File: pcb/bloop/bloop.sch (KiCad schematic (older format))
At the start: 10 parts

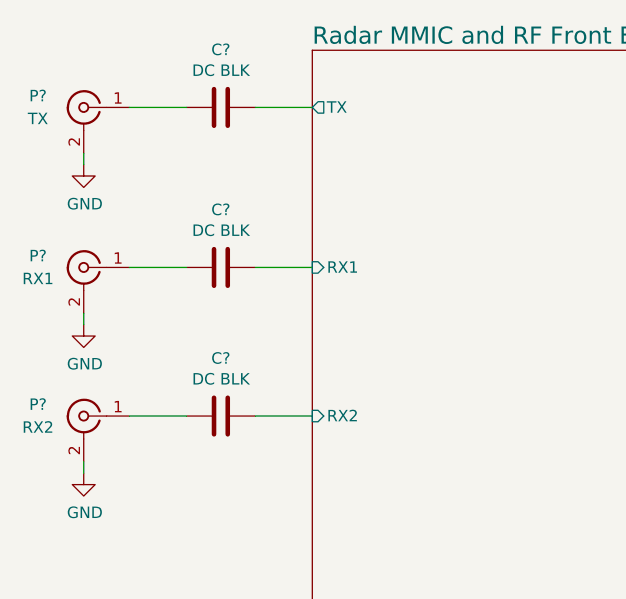
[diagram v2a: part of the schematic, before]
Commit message: Add stubs to RX portion; move blocking caps
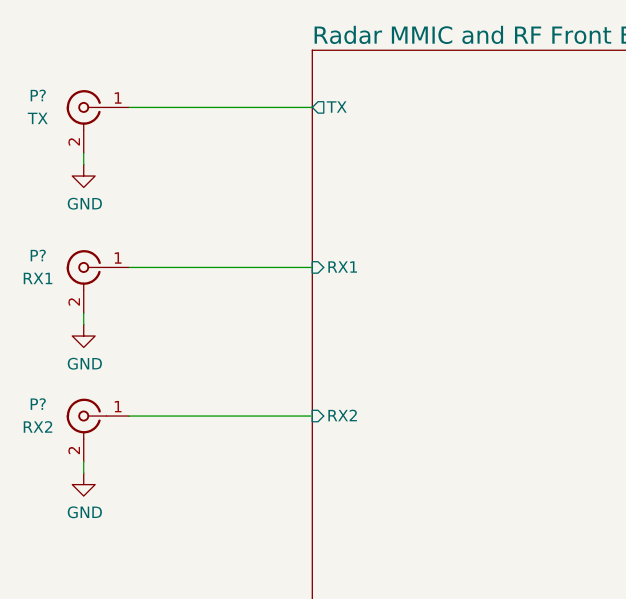
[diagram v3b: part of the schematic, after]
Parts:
- removed C? (x3): DC BLK, symbol Device:C
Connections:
- net Radar MMIC and RF Front End/RX1: now also P?.1 (In)
- net Radar MMIC and RF Front End/RX2: now also P?.1 (In)
- net Radar MMIC and RF Front End/TX: now also P?.1 (In)
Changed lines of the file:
@@
 EESchema Schematic File Version 4
 LIBS:bloop-cache
-EELAYER 29 0
+EELAYER 30 0
 EELAYER END
 $Descr B 17000 11000
@@
 	1    0    0    -1
 $EndComp
+$Comp
+L Mechanical:MountingHole_Pad H?
+U 1 1 5D89D33B
+P 11300 9750
+F 0 "H?" H 11400 9850 50  0000 L CNN
+F 1 "MNT_HOLE" H 11400 9750 50  0000 L CNN
+F 2 "" H 11300 9750 50  0001 C CNN
+F 3 "~" H 11300 9750 50  0001 C CNN
+	1    11300 9750
+	1    0    0    -1
+$EndComp
+$Comp
+L power:GND #PWR?
+U 1 1 5D89E2C2
+P 11300 9850
+F 0 "#PWR?" H 11300 9600 50  0001 C CNN
+F 1 "GND" H 11305 9677 50  0000 C CNN
+F 2 "" H 11300 9850 50  0001 C CNN
+F 3 "" H 11300 9850 50  0001 C CNN
+	1    11300 9850
+	1    0    0    -1
+$EndComp
+$Comp
+L Mechanical:MountingHole_Pad H?
+U 1 1 5D89F708
+P 10300 9750
+F 0 "H?" H 10400 9850 50  0000 L CNN
+F 1 "MNT_HOLE" H 10400 9750 50  0000 L CNN
+F 2 "" H 10300 9750 50  0001 C CNN
+F 3 "~" H 10300 9750 50  0001 C CNN
+	1    10300 9750
+	1    0    0    -1
+$EndComp
+$Comp
+L power:GND #PWR?
+U 1 1 5D89F70E
+P 10300 9850
+F 0 "#PWR?" H 10300 9600 50  0001 C CNN
+F 1 "GND" H 10305 9677 50  0000 C CNN
+F 2 "" H 10300 9850 50  0001 C CNN
+F 3 "" H 10300 9850 50  0001 C CNN
+	1    10300 9850
+	1    0    0    -1
+$EndComp
+$Comp
+L Mechanical:MountingHole_Pad H?
+U 1 1 5D8A33A6
+P 11300 8750
+F 0 "H?" H 11400 8850 50  0000 L CNN
+F 1 "MNT_HOLE" H 11400 8750 50  0000 L CNN
+F 2 "" H 11300 8750 50  0001 C CNN
+F 3 "~" H 11300 8750 50  0001 C CNN
+	1    11300 8750
+	1    0    0    -1
+$EndComp
+$Comp
+L power:GND #PWR?
+U 1 1 5D8A33AC
+P 11300 8850
+F 0 "#PWR?" H 11300 8600 50  0001 C CNN
+F 1 "GND" H 11305 8677 50  0000 C CNN
+F 2 "" H 11300 8850 50  0001 C CNN
+F 3 "" H 11300 8850 50  0001 C CNN
+	1    11300 8850
+	1    0    0    -1
+$EndComp
+$Comp
+L Mechanical:MountingHole_Pad H?
+U 1 1 5D8A33B2
+P 10300 8750
+F 0 "H?" H 10400 8850 50  0000 L CNN
+F 1 "MNT_HOLE" H 10400 8750 50  0000 L CNN
+F 2 "" H 10300 8750 50  0001 C CNN
+F 3 "~" H 10300 8750 50  0001 C CNN
+	1    10300 8750
+	1    0    0    -1
+$EndComp
+$Comp
+L power:GND #PWR?
+U 1 1 5D8A33B8
+P 10300 8850
+F 0 "#PWR?" H 10300 8600 50  0001 C CNN
+F 1 "GND" H 10305 8677 50  0000 C CNN
+F 2 "" H 10300 8850 50  0001 C CNN
+F 3 "" H 10300 8850 50  0001 C CNN
+	1    10300 8850
+	1    0    0    -1
+$EndComp
+Wire Notes Line
+	9600 8400 9600 10300
+Wire Notes Line
+	9600 10300 12000 10300
+Wire Notes Line
+	12000 10300 12000 8400
+Wire Notes Line
+	12000 8400 9600 8400
+Text Notes 10300 8300 0    100  ~ 20
+Mounting Holes
 $Sheet
 S 3900 3400 2200 2750
@@
 F22 "SPI_BGT24_CS" I R 6100 5750 50
 $EndSheet
-$Comp
-L Device:C C?
-U 1 1 5D454FFB
-P 3500 3650
-AR Path="/5D3D1628/5D454FFB" Ref="C?"  Part="1"
-AR Path="/5D454FFB" Ref="C?"  Part="1"
-F 0 "C?" V 3248 3650 50  0000 C CNN
-F 1 "DC BLK" V 3339 3650 50  0000 C CNN
-F 2 "" H 3538 3500 50  0001 C CNN
-F 3 "~" H 3500 3650 50  0001 C CNN
-	1    3500 3650
-	0    1    1    0
-$EndComp
-Wire Wire Line
-	3900 3650 3650 3650
-Wire Wire Line
-	3350 3650 3100 3650
-$Comp
-L Device:C C?
-U 1 1 5D455B2F
-P 3500 4350
-AR Path="/5D3D1628/5D455B2F" Ref="C?"  Part="1"
-AR Path="/5D455B2F" Ref="C?"  Part="1"
-F 0 "C?" V 3248 4350 50  0000 C CNN
-F 1 "DC BLK" V 3339 4350 50  0000 C CNN
-F 2 "" H 3538 4200 50  0001 C CNN
-F 3 "~" H 3500 4350 50  0001 C CNN
-	1    3500 4350
-	0    1    1    0
-$EndComp
-Wire Wire Line
-	3900 4350 3650 4350
-Wire Wire Line
-	3350 4350 3100 4350
-$Comp
-L Device:C C?
-U 1 1 5D455FA2
-P 3500 5000
-AR Path="/5D3D1628/5D455FA2" Ref="C?"  Part="1"
-AR Path="/5D455FA2" Ref="C?"  Part="1"
-F 0 "C?" V 3248 5000 50  0000 C CNN
-F 1 "DC BLK" V 3339 5000 50  0000 C CNN
-F 2 "" H 3538 4850 50  0001 C CNN
-F 3 "~" H 3500 5000 50  0001 C CNN
-	1    3500 5000
-	0    1    1    0
-$EndComp
-Wire Wire Line
-	3900 5000 3650 5000
-Wire Wire Line
-	3350 5000 3100 5000
-$Comp
-L Mechanical:MountingHole_Pad H?
-U 1 1 5D89D33B
-P 11300 9750
-F 0 "H?" H 11400 9850 50  0000 L CNN
-F 1 "MNT_HOLE" H 11400 9750 50  0000 L CNN
-F 2 "" H 11300 9750 50  0001 C CNN
-F 3 "~" H 11300 9750 50  0001 C CNN
-	1    11300 9750
-	1    0    0    -1
-$EndComp
-$Comp
-L power:GND #PWR?
-U 1 1 5D89E2C2
-P 11300 9850
-F 0 "#PWR?" H 11300 9600 50  0001 C CNN
-F 1 "GND" H 11305 9677 50  0000 C CNN
-F 2 "" H 11300 9850 50  0001 C CNN
-F 3 "" H 11300 9850 50  0001 C CNN
-	1    11300 9850
-	1    0    0    -1
-$EndComp
-$Comp
-L Mechanical:MountingHole_Pad H?
-U 1 1 5D89F708
-P 10300 9750
-F 0 "H?" H 10400 9850 50  0000 L CNN
-F 1 "MNT_HOLE" H 10400 9750 50  0000 L CNN
-F 2 "" H 10300 9750 50  0001 C CNN
-F 3 "~" H 10300 9750 50  0001 C CNN
-	1    10300 9750
-	1    0    0    -1
-$EndComp
-$Comp
-L power:GND #PWR?
-U 1 1 5D89F70E
-P 10300 9850
-F 0 "#PWR?" H 10300 9600 50  0001 C CNN
-F 1 "GND" H 10305 9677 50  0000 C CNN
-F 2 "" H 10300 9850 50  0001 C CNN
-F 3 "" H 10300 9850 50  0001 C CNN
-	1    10300 9850
-	1    0    0    -1
-$EndComp
-$Comp
-L Mechanical:MountingHole_Pad H?
-U 1 1 5D8A33A6
-P 11300 8750
-F 0 "H?" H 11400 8850 50  0000 L CNN
-F 1 "MNT_HOLE" H 11400 8750 50  0000 L CNN
-F 2 "" H 11300 8750 50  0001 C CNN
-F 3 "~" H 11300 8750 50  0001 C CNN
-	1    11300 8750
-	1    0    0    -1
-$EndComp
-$Comp
-L power:GND #PWR?
-U 1 1 5D8A33AC
-P 11300 8850
-F 0 "#PWR?" H 11300 8600 50  0001 C CNN
-F 1 "GND" H 11305 8677 50  0000 C CNN
-F 2 "" H 11300 8850 50  0001 C CNN
-F 3 "" H 11300 8850 50  0001 C CNN
-	1    11300 8850
-	1    0    0    -1
-$EndComp
-$Comp
-L Mechanical:MountingHole_Pad H?
-U 1 1 5D8A33B2
-P 10300 8750
-F 0 "H?" H 10400 8850 50  0000 L CNN
-F 1 "MNT_HOLE" H 10400 8750 50  0000 L CNN
-F 2 "" H 10300 8750 50  0001 C CNN
-F 3 "~" H 10300 8750 50  0001 C CNN
-	1    10300 8750
-	1    0    0    -1
-$EndComp
-$Comp
-L power:GND #PWR?
-U 1 1 5D8A33B8
-P 10300 8850
-F 0 "#PWR?" H 10300 8600 50  0001 C CNN
-F 1 "GND" H 10305 8677 50  0000 C CNN
-F 2 "" H 10300 8850 50  0001 C CNN
-F 3 "" H 10300 8850 50  0001 C CNN
-	1    10300 8850
-	1    0    0    -1
-$EndComp
-Wire Notes Line
-	9600 8400 9600 10300
-Wire Notes Line
-	9600 10300 12000 10300
-Wire Notes Line
-	12000 10300 12000 8400
-Wire Notes Line
-	12000 8400 9600 8400
-Text Notes 10300 8300 0    100  ~ 20
-Mounting Holes
+Wire Wire Line
+	3900 5000 3100 5000
+Wire Wire Line
+	3900 4350 3100 4350
+Wire Wire Line
+	3900 3650 3100 3650
 $EndSCHEMATC
